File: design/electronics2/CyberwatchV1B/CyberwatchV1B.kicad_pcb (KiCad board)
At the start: 2 copper layers, 32 parts, among them J1 Micro_SD_Card, J10 Conn_01x07_M_power, J2 Conn_01x08_Display, J3 Conn_01x02_Socket, J5 Conn_01x03_M_input_left, J6 Conn_01x07_M_input_right, J7 Conn_01x03_IL_main, J8 Conn_01x07_IR_main, J9 Conn_01x07_PWR_main, Q1 AO3401A, SW1 SW_Push, SW2 SW_Push, SW4 SW_Push, SW6 SW_power, U1 XIAO-ESP32-S3-Plus-SMD, U2 MCP23017x-x-ML, U3 DS3231MZ, U4 MAX17048, U5 MT6701CT

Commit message: pcb design
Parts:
- removed J10: Conn_01x07_M_power, Connector_JST:JST_SH_SM07B-SRSS-TB_1x07-1MP_P1.00mm_Horizontal
- removed J9: Conn_01x07_PWR_main, Connector_JST:JST_SH_SM07B-SRSS-TB_1x07-1MP_P1.00mm_Horizontal
- removed the R2 at (101.5, 142.8)
- removed SW6: SW_power, Button_Switch_SMD:SW_DIP_SPSTx01_Slide_Copal_CHS-01A_W5.08mm_P1.27mm_JPin
- removed the U4 at (93.2, 137.5)
- added C3: 100nF, Capacitor_SMD:C_0603_1608Metric, F.Cu at (149.0, 110.8)
- added C4: 100nF, Capacitor_SMD:C_0603_1608Metric, F.Cu at (183.1, 92.5)
- added R4: 10k, Resistor_SMD:R_0603_1608Metric, F.Cu at (159.0, 108.2)
- added SW1: SW_power, Button_Switch_SMD:SW_DIP_SPSTx01_Slide_Copal_CHS-01A_W5.08mm_P1.27mm_JPin, F.Cu at (162.5, 87.5)
- added U2: DS3231MZ, Package_SO:SOIC-8_3.9x4.9mm_P1.27mm, F.Cu at (162.5, 83.0)
- J1: renamed from J5; value Conn_01x03_M_input_left -> Conn_01x02_M_Battery; footprint Connector_JST:JST_SH_SM03B-SRSS-TB_1x03-1MP_P1.00mm_Horizontal -> Connector_JST:JST_PH_S2B-PH-SM4-TB_1x02-1MP_P2.00mm_Horizontal
- J2: value Conn_01x08_Display -> Conn_01x03_M_input_left; footprint Connector_JST:JST_GH_SM08B-GHS-TB_1x08-1MP_P1.25mm_Horizontal -> Connector_JST:JST_SH_SM03B-SRSS-TB_1x03-1MP_P1.00mm_Horizontal
- J3: value Conn_01x02_Socket -> Conn_01x07_M_input_right; footprint Connector_JST:JST_PH_S2B-PH-SM4-TB_1x02-1MP_P2.00mm_Horizontal -> Connector_JST:JST_SH_SM07B-SRSS-TB_1x07-1MP_P1.00mm_Horizontal
- J4: renamed from J1; value Micro_SD_Card -> Conn_01x08_M_Display; footprint Connector_Card:microSD_HC_Molex_47219-2001 -> Connector_JST:JST_GH_SM08B-GHS-TB_1x08-1MP_P1.25mm_Horizontal
- J5: renamed from J6; value Conn_01x07_M_input_right -> Micro_SD_Card; footprint Connector_JST:JST_SH_SM07B-SRSS-TB_1x07-1MP_P1.00mm_Horizontal -> Connector_Card:microSD_HC_Molex_47219-2001
- R1: value 33 -> 100k
- R10: renamed from R7; value 10k -> 4.7k
- R2: renamed from R8; value 4.7k -> 33
- R3: renamed from R9; value 4.7k -> 10k
- R9: renamed from R6; value 10k -> 4.7k
- U1: renamed from U2; value MCP23017x-x-ML -> MAX17048; footprint Package_DFN_QFN:QFN-28-1EP_6x6mm_P0.65mm_EP4.25x4.25mm -> Package_DFN_QFN:TDFN-8-1EP_2x2mm_P0.5mm_EP0.8x1.2mm
- U4: renamed from U3; value DS3231MZ -> MCP23017x-x-ML; footprint Package_SO:SOIC-8_3.9x4.9mm_P1.27mm -> Package_DFN_QFN:QFN-28-1EP_6x6mm_P0.65mm_EP4.25x4.25mm
- moved Q1 87.4 mm to (173.0, 110.9), turned to -90 degrees
- moved R1 86.0 mm to (173.5, 100.7)
- moved R2 84.7 mm to (173.5, 95.2), turned to -90 degrees
- moved J3 82.9 mm to (170.0, 119.7), turned to 90 degrees
- moved J4 80.9 mm to (145.8, 118.1), turned to -90 degrees
- moved J1 79.7 mm to (171.2, 85.2), turned to 180 degrees
- moved SW3 77.3 mm to (131.0, 112.0), turned to 90 degrees
- moved SW2 76.1 mm to (130.9, 94.5), turned to 90 degrees
- moved R7 71.5 mm to (168.5, 110.2), turned to -90 degrees
- moved R3 68.5 mm to (155.8, 105.0), turned to 180 degrees
- moved R6 68.5 mm to (161.7, 108.5), turned to 180 degrees
- moved R10 61.2 mm to (155.0, 108.2)
- moved J6 61.2 mm to (131.5, 103.5), turned to 90 degrees
- moved R8 59.6 mm to (157.0, 108.2), turned to -90 degrees
- moved BT1 55.9 mm to (165.5, 99.5), turned to 90 degrees
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- renumbered J7 to J6, J8 to J7, R10 to R5, R3 to R6, R4 to R7, R5 to R8, SW1 to SW2, SW2 to SW3, U1 to U3
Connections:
- net /main/VBAT_SWITCHED renamed /main/D
- C1 pad 1: +3.3V -> Net-(U2-VCC)
- C1 pad 2: Net-(U2-V_{DD}) -> /main/S
- C2 pad 1: Net-(U3-VCC) -> GND
- C2 pad 2: /main/VBAT_RAW -> /main/S
- J1 pad 1: GND -> /main/S
- J1 pad 2: /main/BTN_1 -> GND
- J2 pad 1: +3.3V -> GND
- J2 pad 2: GND -> /main/BTN_1
- J2 pad 3: /main/SPI_MOSI -> /main/BTN_2
- J3 pad 1: /main/VBAT_RAW -> GND
- J3 pad 2: GND -> +3.3V
- J4 pad 1: Net-(J1-DAT2) -> +3.3V
- J4 pad 2: Net-(J1-DAT3/CD) -> GND
- J4 pad 3: Net-(J1-CMD) -> /main/SPI_MOSI
- J4 pad 4: +3.3V -> /main/SPI_CLK
- J4 pad 5: /main/SPI_CLK -> Net-(J4-CS)
- J4 pad 6: GND -> Net-(J4-Pin_6)
- J4 pad 7: Net-(J1-DAT0) -> Net-(J4-Pin_7)
- J4 pad 8: Net-(J1-DAT1) -> Net-(J4-Pin_8)
- J5 pad 1: GND -> Net-(J5-DAT2)
- J5 pad 2: +3.3V -> Net-(J5-DAT3/CD)
- J5 pad 3: /SDA -> Net-(J5-CMD)
- J5 pad 4: /SCL -> +3.3V
- J5 pad 5: /input_right/BTN_3 -> /main/SPI_CLK
- J5 pad 6: /input_right/BTN_4 -> GND
- J5 pad 7: GND -> Net-(J5-DAT0)
- J7 pad 3: /SDA -> /input_right/SDA
- J7 pad 4: /SCL -> /input_right/SCL
- Q1 pad 1: /power/G -> /main/G
- Q1 pad 2: /main/VBAT_RAW -> /main/S
- R1 pad 1: /main/VBAT_RAW -> /main/S
- R1 pad 2: /power/G -> /main/G
- R10 pad 1: +3.3V -> /input_right/SCL
- R10 pad 2: Net-(J1-DAT2) -> Net-(U3-D5)
- R2 pad 1: /SDA -> Net-(SW1-A)
- R2 pad 2: Net-(U1-D4) -> /main/G
- R3 pad 1: /SCL -> +3.3V
- R3 pad 2: Net-(U1-D5) -> Net-(U2-~{RST})
- R5 pad 1: +3.3V -> Net-(U3-D9)
- R5 pad 2: Net-(U3-~{RST}) -> Net-(J5-DAT3/CD)
- R6 pad 1: Net-(U1-D9) -> /main/SPI_MOSI
- R6 pad 2: Net-(J1-DAT3/CD) -> Net-(J5-CMD)
- R7 pad 1: /main/SPI_MOSI -> /main/SPI_MISO
- R7 pad 2: Net-(J1-CMD) -> Net-(J5-DAT0)
- R8 pad 1: /main/SPI_MISO -> +3.3V
- R8 pad 2: Net-(J1-DAT0) -> Net-(J5-DAT1)
- R9 pad 1: +3.3V -> /input_right/SDA
- R9 pad 2: Net-(J1-DAT1) -> Net-(U3-D4)
- U1 pad 1: unconnected-(U2-GPB4-Pad1) -> /main/S
- U1 pad 3: unconnected-(U2-GPB6-Pad3) -> GND
- U1 pad 4: unconnected-(U2-GPB7-Pad4) -> GND
- U1 pad 5: Net-(U2-V_{DD}) -> /main/PWR_ALRT
- U1 pad 6: GND -> /input_right/SDA
- U1 pad 7: unconnected-(U2-NC-Pad7) -> /input_right/SCL
- U1 pad 8: /SCL -> GND
- U1 pad 9: /SDA -> (no net)
- U3 pad 10: Net-(U1-D9) -> Net-(U3-D9)
- U3 pad 2: Net-(J2-CS) -> Net-(J4-CS)
- U3 pad 4: Net-(J2-Pin_6) -> Net-(J4-Pin_6)
- U3 pad 5: Net-(U1-D4) -> Net-(U3-D4)
- U3 pad 6: Net-(U1-D5) -> Net-(U3-D5)
- U4 pad 2: Net-(U3-VCC) -> unconnected-(U4-GPB5-Pad2)
- U4 pad 4: Net-(U3-~{RST}) -> unconnected-(U4-GPB7-Pad4)
- U4 pad 5: GND -> Net-(U4-V_{DD})
- U4 pad 6: Net-(BT1-+) -> GND
- U4 pad 7: /SDA -> unconnected-(U4-NC-Pad7)
- U4 pad 8: /SCL -> /input_right/SCL
- U5 pad 1: +3.3V -> Net-(U5-VDD)
- U5 pad 6: /SDA -> /input_right/SDA
- U5 pad 7: /SCL -> /input_right/SCL
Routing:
- net GND: track 0.00 -> 274.3 mm, vias 0 -> 13
- net /input_right/SCL: track 0.00 -> 105.7 mm, vias 0 -> 5
- net +3.3V: track 0.00 -> 94.9 mm, vias 0 -> 4
- net /input_right/SDA: track 0.00 -> 78.5 mm, vias 0 -> 8
- net /main/PWR_ALRT: track 0.00 -> 76.2 mm, vias 0 -> 2
- net /input_right/BTN_3: track 0.00 -> 64.2 mm, vias 0 -> 5
- net /input_right/BTN_4: track 0.00 -> 60.3 mm, vias 0 -> 4
- net /main/SPI_CLK: track 0.00 -> 58.3 mm
- net Net-(U3-D5): track 0.00 -> 57.0 mm, vias 0 -> 2
- net /main/S: track 0.00 -> 46.6 mm, vias 0 -> 4
- net /main/SPI_MOSI: track 0.00 -> 46.4 mm, vias 0 -> 3
- net Net-(J4-CS): track 0.00 -> 40.6 mm
- net Net-(J5-DAT0): track 0.00 -> 35.8 mm, vias 0 -> 4
- net /main/D: track 0.00 -> 35.5 mm, vias 0 -> 2
- net /main/BTN_2: track 0.00 -> 35.1 mm, vias 0 -> 2
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- added copper zone on F.Cu, net GND
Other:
- board outline added: 60 x 45.5 mm

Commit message: pcb design 2
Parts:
- moved R5 8.34 mm to (174.5, 114.0)
- moved R1 6.83 mm to (173.7, 107.5), turned to 0 degrees
- moved R2 3.67 mm to (173.5, 91.5), turned to 0 degrees
- moved J6 1.02 mm to (130.5, 103.7)
- moved J1 0.35 mm to (171.2, 85.5)
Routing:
- net GND: track 274.3 -> 244.6 mm, vias 13 -> 15
- net +3.3V: track 94.9 -> 80.8 mm
- net Net-(U3-D4): track 30.4 -> 21.0 mm, vias 3 -> 2
- net Net-(U3-D9): track 22.5 -> 29.8 mm, vias 2 -> 4
- net /input_right/BTN_4: track 60.3 -> 53.3 mm, vias 4 -> 7
- net Net-(J5-DAT3/CD): track 26.1 -> 30.6 mm
- net /input_right/SCL: track 105.7 -> 101.9 mm
- net Net-(SW1-A): track 17.3 -> 14.2 mm
- net Net-(BT1-+): track 28.4 -> 31.5 mm
- net /main/SPI_CLK: track 58.3 -> 55.7 mm
- net /main/G: track 16.9 -> 19.2 mm, vias 2 -> 0
- net /main/S: track 46.6 -> 48.2 mm
- net /input_right/SDA: track 78.5 -> 77.3 mm, vias 8 -> 7
- net /main/BTN_1: track 30.4 -> 31.4 mm, vias 2 -> 4
- net Net-(U2-VCC): track 10.1 -> 9.22 mm
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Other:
- board text added: "CyberwatchV1B Created 31/08/26(UK) Edward Swingler"

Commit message: PCB design finalisation
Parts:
- added REF**: Fiducial_0.5mm_Mask1.5mm, Fiducial:Fiducial_0.5mm_Mask1.5mm, F.Cu at (191.9, 115.0)
- added REF**: Fiducial_0.5mm_Mask1.5mm, Fiducial:Fiducial_0.5mm_Mask1.5mm, F.Cu at (123.2, 115.5)
- added REF**: Fiducial_0.5mm_Mask1.5mm, Fiducial:Fiducial_0.5mm_Mask1.5mm, F.Cu at (173.5, 95.0)
- added REF**: Fiducial_0.5mm_Mask1.5mm, Fiducial:Fiducial_0.5mm_Mask1.5mm, F.Cu at (140.5, 110.5)
- added REF**: Fiducial_0.5mm_Mask1.5mm, Fiducial:Fiducial_0.5mm_Mask1.5mm, F.Cu at (191.9, 111.5)
- added REF**: MountingHole_2.1mm, MountingHole:MountingHole_2.1mm, F.Cu at (190.5, 89.0)
- added REF**: Fiducial_0.5mm_Mask1.5mm, Fiducial:Fiducial_0.5mm_Mask1.5mm, F.Cu at (118.8, 90.0)
- added REF**: MountingHole_2.1mm, MountingHole:MountingHole_2.1mm, F.Cu at (122.2, 88.5)
- added REF**: MountingHole_2.1mm, MountingHole:MountingHole_2.1mm, F.Cu at (119.8, 117.0)
- added REF**: Fiducial_0.5mm_Mask1.5mm, Fiducial:Fiducial_0.5mm_Mask1.5mm, F.Cu at (118.8, 98.5)
- added REF**: MountingHole_2.1mm, MountingHole:MountingHole_2.1mm, F.Cu at (189.2, 119.5)
- added REF**: Fiducial_0.5mm_Mask1.5mm, Fiducial:Fiducial_0.5mm_Mask1.5mm, F.Cu at (186.9, 92.0)
- added REF**: Fiducial_0.5mm_Mask1.5mm, Fiducial:Fiducial_0.5mm_Mask1.5mm, F.Cu at (160.0, 92.0)
- moved J6 9.76 mm to (120.8, 103.2)
- moved SW3 9.76 mm to (121.2, 111.5)
- moved SW2 9.76 mm to (121.2, 94.0)
- moved C4 7.10 mm to (190.2, 92.5)
- moved U5 6.58 mm to (189.6, 96.4)
- moved J7 6.44 mm to (189.4, 105.2)
- moved SW4 5.58 mm to (188.7, 113.9)
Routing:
- net GND: track 244.6 -> 231.5 mm
- net Net-(U3-D5): track 57.0 -> 51.1 mm
- net /main/G: track 19.2 -> 21.0 mm
- net /input_right/SDA: track 77.3 -> 79.0 mm
- net /input_right/BTN_3: track 63.9 -> 65.5 mm, vias 4 -> 2
- net Net-(U5-VDD): track 2.63 -> 3.60 mm
- net /input_right/BTN_4: track 53.3 -> 52.5 mm
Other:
- board size 60 x 45.5 mm -> 77.2 x 45.5 mm

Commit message: pcb fabrication prep
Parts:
- renumbered REF** to FID1, REF** to FID2, REF** to FID3, REF** to FID4, REF** to FID5, REF** to FID6, REF** to FID7, REF** to FID8, REF** to FID9
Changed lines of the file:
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@@
 		(filling no)
 		(pcbplotparams
-			(layerselection 0x00000000_00000000_55555555_5755f5ff)
+			(layerselection 0x00000000_00000000_55555555_f755ffff)
 			(plot_on_all_layers_selection 0x00000000_00000000_00000000_00000000)
 			(disableapertmacros no)
@@
 			(outputformat 1)
 			(mirror no)
-			(drillshape 1)
+			(drillshape 0)
 			(scaleselection 1)
-			(outputdirectory "")
+			(outputdirectory "gbr/")
 		)
 	)
@@
 		(descr "Fiducial, circular marking, 0.5mm bare copper, 1.5mm soldermask opening")
 		(tags "fiducial")
-		(property "Reference" "REF**"
+		(property "Reference" "FID9"
 			(at -1 1 0)
 			(layer "F.SilkS")
@@
 		(descr "Fiducial, circular marking, 0.5mm bare copper, 1.5mm soldermask opening")
 		(tags "fiducial")
-		(property "Reference" "REF**"
+		(property "Reference" "FID1"
 			(at -1 1 0)
 			(layer "F.SilkS")
@@
 		(descr "Fiducial, circular marking, 0.5mm bare copper, 1.5mm soldermask opening")
 		(tags "fiducial")
-		(property "Reference" "REF**"
+		(property "Reference" "FID2"
 			(at -1 1 0)
 			(layer "F.SilkS")
@@
 		(descr "Fiducial, circular marking, 0.5mm bare copper, 1.5mm soldermask opening")
 		(tags "fiducial")
-		(property "Reference" "REF**"
+		(property "Reference" "FID7"
 			(at -1 1 0)
 			(layer "F.SilkS")
@@
 		(descr "Fiducial, circular marking, 0.5mm bare copper, 1.5mm soldermask opening")
 		(tags "fiducial")
-		(property "Reference" "REF**"
+		(property "Reference" "FID4"
 			(at -1 1 0)
 			(layer "F.SilkS")
@@
 		(descr "Fiducial, circular marking, 0.5mm bare copper, 1.5mm soldermask opening")
 		(tags "fiducial")
-		(property "Reference" "REF**"
+		(property "Reference" "FID3"
 			(at -1 1 0)
 			(layer "F.SilkS")
@@
 		(descr "Fiducial, circular marking, 0.5mm bare copper, 1.5mm soldermask opening")
 		(tags "fiducial")
-		(property "Reference" "REF**"
+		(property "Reference" "FID5"
 			(at -1 1 0)
 			(layer "F.SilkS")
@@
 		(descr "Fiducial, circular marking, 0.5mm bare copper, 1.5mm soldermask opening")
 		(tags "fiducial")
-		(property "Reference" "REF**"
+		(property "Reference" "FID6"
 			(at -1 1 0)
 			(layer "F.SilkS")
@@
 		(descr "Fiducial, circular marking, 0.5mm bare copper, 1.5mm soldermask opening")
 		(tags "fiducial")
-		(property "Reference" "REF**"
+		(property "Reference" "FID8"
 			(at -1 1 0)
 			(layer "F.SilkS")

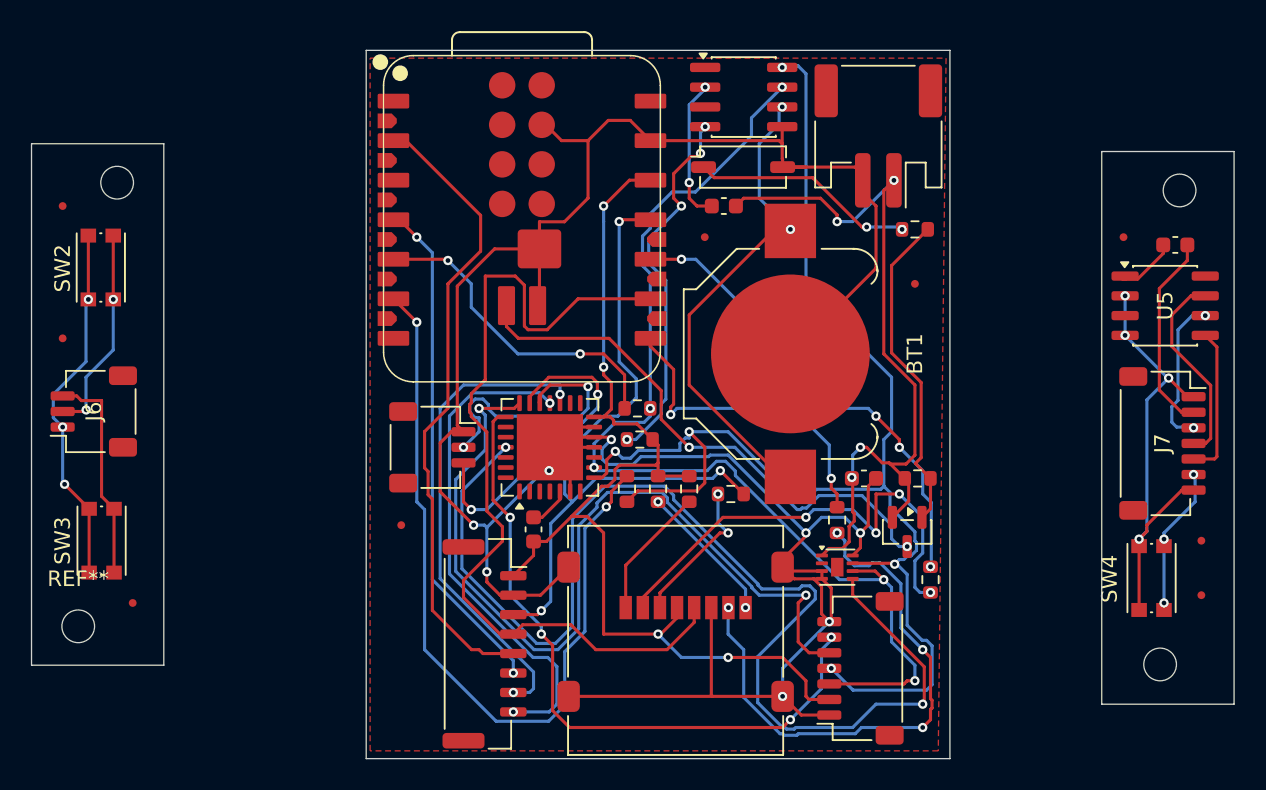
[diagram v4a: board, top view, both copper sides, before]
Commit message: pcb fabrication adjustment: no via in pads
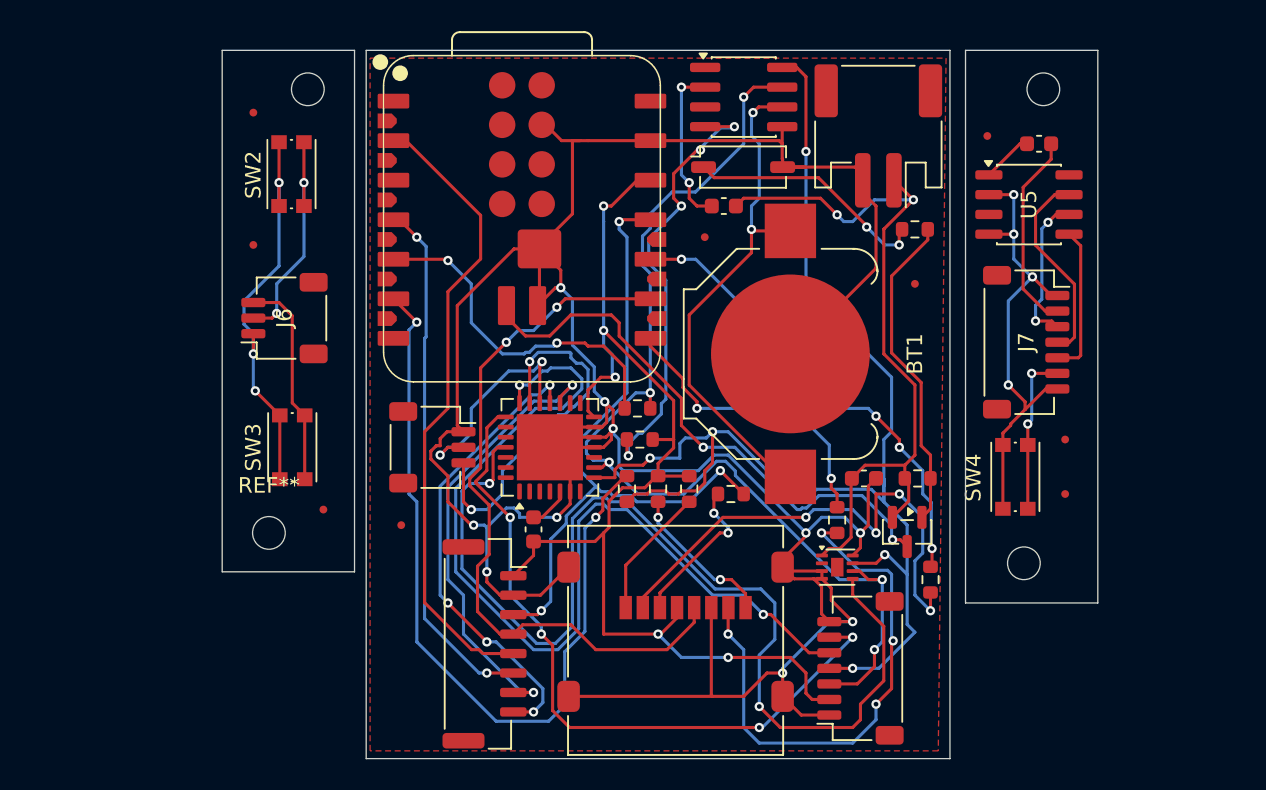
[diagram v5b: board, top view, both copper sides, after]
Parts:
- moved FID1 13.6 mm to (131.0, 84.0)
- moved FID2 13.6 mm to (131.0, 92.5)
- moved FID3 13.6 mm to (135.5, 109.5)
- moved J6 13.6 mm to (133.0, 97.2)
- moved REF** 13.6 mm to (134.5, 82.5)
- moved REF** 13.6 mm to (132.0, 111.0)
- moved SW3 13.6 mm to (133.5, 105.5)
- moved SW2 13.6 mm to (133.4, 88.0)
- moved C4 10.9 mm to (181.5, 86.0)
- moved FID7 10.9 mm to (178.1, 85.5)
- moved FID8 10.9 mm to (183.1, 105.0)
- moved FID9 10.9 mm to (183.1, 108.5)
- moved J7 10.9 mm to (180.6, 98.8)
- moved REF** 10.9 mm to (181.8, 82.5)
- moved REF** 10.9 mm to (180.5, 113.0)
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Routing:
- net GND: track 231.5 -> 260.5 mm, vias 15 -> 17
- net /main/SPI_CLK: track 55.7 -> 46.6 mm, vias 0 -> 2
- net /main/PWR_ALRT: track 75.8 -> 67.7 mm
- net +3.3V: track 81.2 -> 86.5 mm, vias 4 -> 5
- net Net-(U2-~{RST}): track 24.1 -> 29.1 mm
- net /input_right/BTN_3: track 65.5 -> 70.4 mm
- net /input_right/BTN_4: track 52.5 -> 56.1 mm, vias 7 -> 6
- net /input_right/SCL: track 102.1 -> 98.7 mm
- net /main/SPI_MOSI: track 46.4 -> 43.6 mm
- net Net-(J4-Pin_8): track 32.3 -> 30.1 mm, vias 2 -> 4
- net /main/BTN_2: track 35.2 -> 37.2 mm
- net Net-(J5-DAT3/CD): track 30.6 -> 32.5 mm
- net Net-(J4-Pin_7): track 31.4 -> 29.4 mm
- net /main/SPI_MISO: track 21.1 -> 19.4 mm
- net Net-(BT1-+): track 31.5 -> 33.1 mm
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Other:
- board size 77.2 x 45.5 mm -> 56.2 x 45.5 mm
